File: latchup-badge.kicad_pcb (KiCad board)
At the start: 2 copper layers, 101.6 x 71.1 mm, 42 parts, among them J1 USB_B_Micro, J2 Connector_Generic:Conn_02x06_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, J3 Connector_Generic:Conn_02x06_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, J4 Connector_Generic:Conn_02x05_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, SW1 SW_Push, SW2 SW_Push, U1 ICE40UP5K-SG48ITR, U2 TLV70012_SOT23-5, U3 TLV70033_SOT23-5, U4 M25PX32-VMW, X1 ASE-12.000MHz

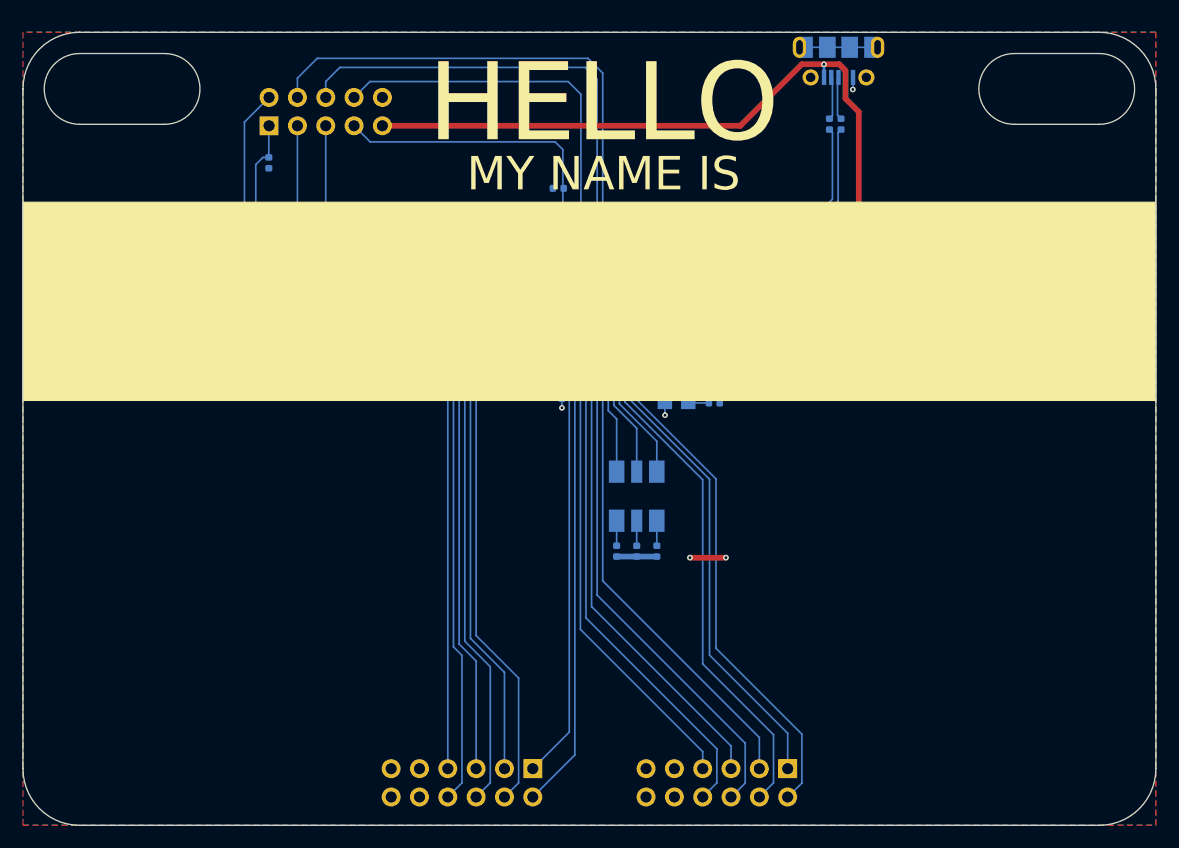
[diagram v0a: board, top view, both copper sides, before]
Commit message: Switch to USB-C connector and shrink board
Signed-off-by: Michael Welling <mwelling@ieee.org>
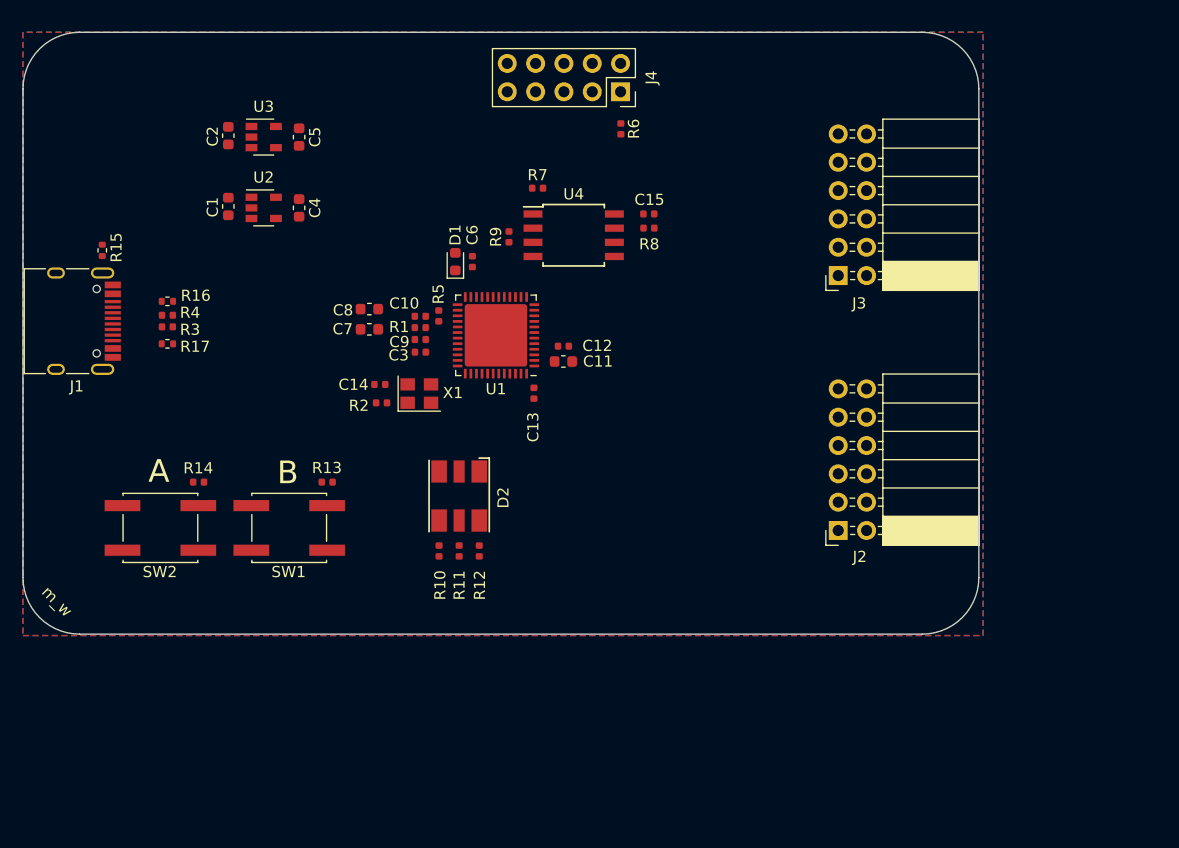
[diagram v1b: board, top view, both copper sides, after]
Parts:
- added R15: 1M, Resistor_SMD:R_0402_1005Metric, F.Cu at (83.3, 70.4)
- added R16: 5.1K, Resistor_SMD:R_0402_1005Metric, F.Cu at (89.2, 74.9)
- added R17: 5.1K, Resistor_SMD:R_0402_1005Metric, F.Cu at (89.2, 78.7)
- C1, C10, C11, C12, C13, C14, C15, C2, C3, C4, C5, C6, C7, C8, C9, D1, D2, J2, J3, J4, R1, R10, R11, R12, R13, R14, R2, R3, R4, R5, R6, R7, R8, R9, SW1, SW2, U1, U2, U3, U4, X1: moved to F.Cu
- J1: value USB_B_Micro -> USB_C_Receptacle_USB2.0; footprint Connector_USB:USB_Micro-B_Molex-105017-0001 -> Connector_USB:USB_C_Receptacle_HRO_TYPE-C-31-M-12; moved to F.Cu
- moved SW2 85.1 mm to (88.5, 95.2), turned to 180 degrees
- moved R14 78.4 mm to (92.0, 91.1), turned to 180 degrees
- moved J1 73.0 mm to (80.2, 76.7), turned to -90 degrees
- moved R3 63.1 mm to (89.2, 77.2), turned to 180 degrees
- moved SW1 62.8 mm to (100.1, 95.2), turned to 180 degrees
- moved R4 61.8 mm to (89.2, 76.2), turned to 180 degrees
- moved C1 56.5 mm to (94.6, 66.4)
- moved C2 56.5 mm to (94.6, 60.1)
- moved R13 56.4 mm to (103.5, 91.1), turned to 180 degrees
- moved J3 52.0 mm to (149.3, 72.6), turned to 180 degrees
- moved U2 50.4 mm to (97.8, 66.5), turned to 0 degrees
- moved U3 50.4 mm to (97.8, 60.2), turned to 0 degrees
- moved C4 44.3 mm to (101.0, 66.5)
- moved C5 44.3 mm to (101.0, 60.2)
- moved C7 32.0 mm to (107.3, 77.4), turned to 180 degrees
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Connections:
- R3 pad 1: /USBD+ -> /USBD-
- R3 pad 2: Net-(J1-Pad3) -> Net-(R3-Pad2)
- R4 pad 1: /USBD- -> /USBD+
- R4 pad 2: Net-(J1-Pad2) -> Net-(R4-Pad2)
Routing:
- net +5V: track 81.3 -> 0.00 mm, vias 2 -> 0
- net /J3_P8: track 54.4 -> 0.00 mm
- net /J3_P6: track 53.0 -> 0.00 mm
- net /J3_P7: track 52.9 -> 0.00 mm
- net /J3_P5: track 50.6 -> 0.00 mm
- net /J3_P4: track 50.6 -> 0.00 mm
- net /TX: track 50.5 -> 0.00 mm
- net /J3_P3: track 49.3 -> 0.00 mm
- net /BTN_A: track 48.9 -> 0.00 mm, vias 2 -> 0
- net /CDONE: track 47.2 -> 0.00 mm, vias 2 -> 0
- net /RX: track 46.3 -> 0.00 mm
- net /ICE40_SPI_SI: track 45.8 -> 0.00 mm
- net /J2_P2: track 45.3 -> 0.00 mm
- net /J2_P4: track 44.0 -> 0.00 mm
- net /J2_P6: track 44.0 -> 0.00 mm
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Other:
- board size 101.6 x 71.1 mm -> 85.7 x 54 mm
- board text removed: "HELLO"
- board text removed: "MY NAME IS"
- board text removed: "PCB Sponsored by:"

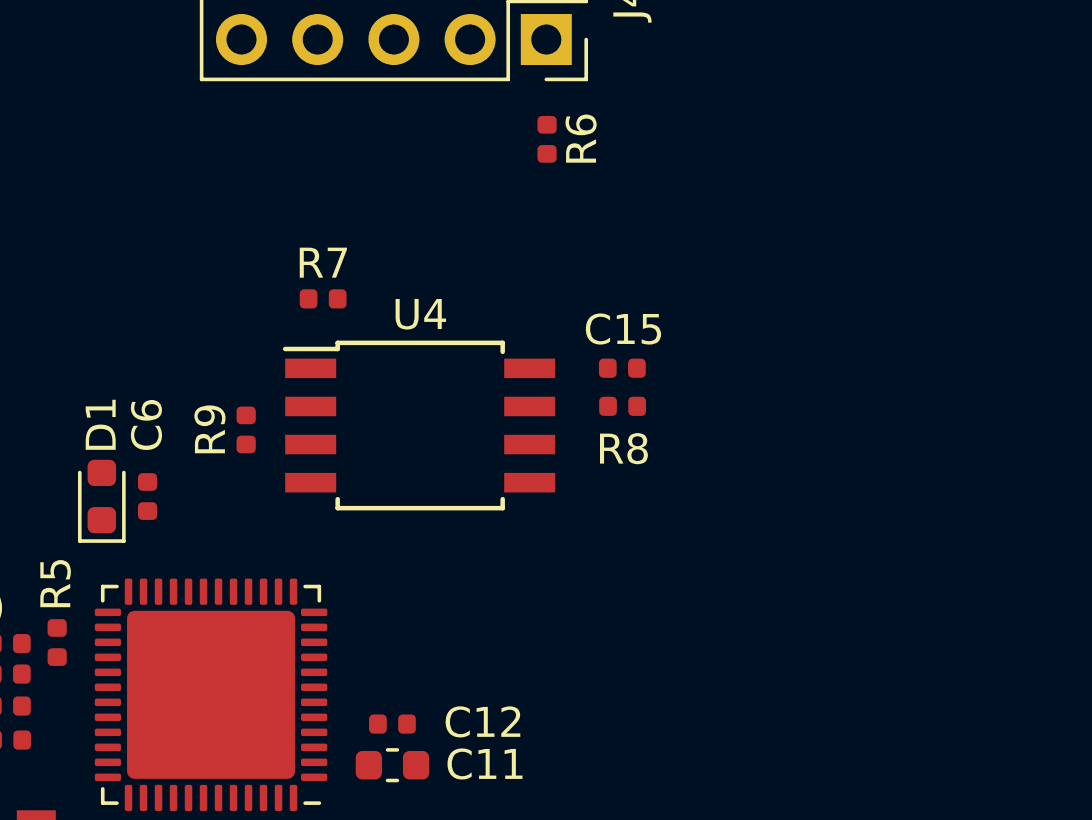
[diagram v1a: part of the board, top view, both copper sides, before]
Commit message: Add PSRAM
Signed-off-by: Michael Welling <mwelling@ieee.org>
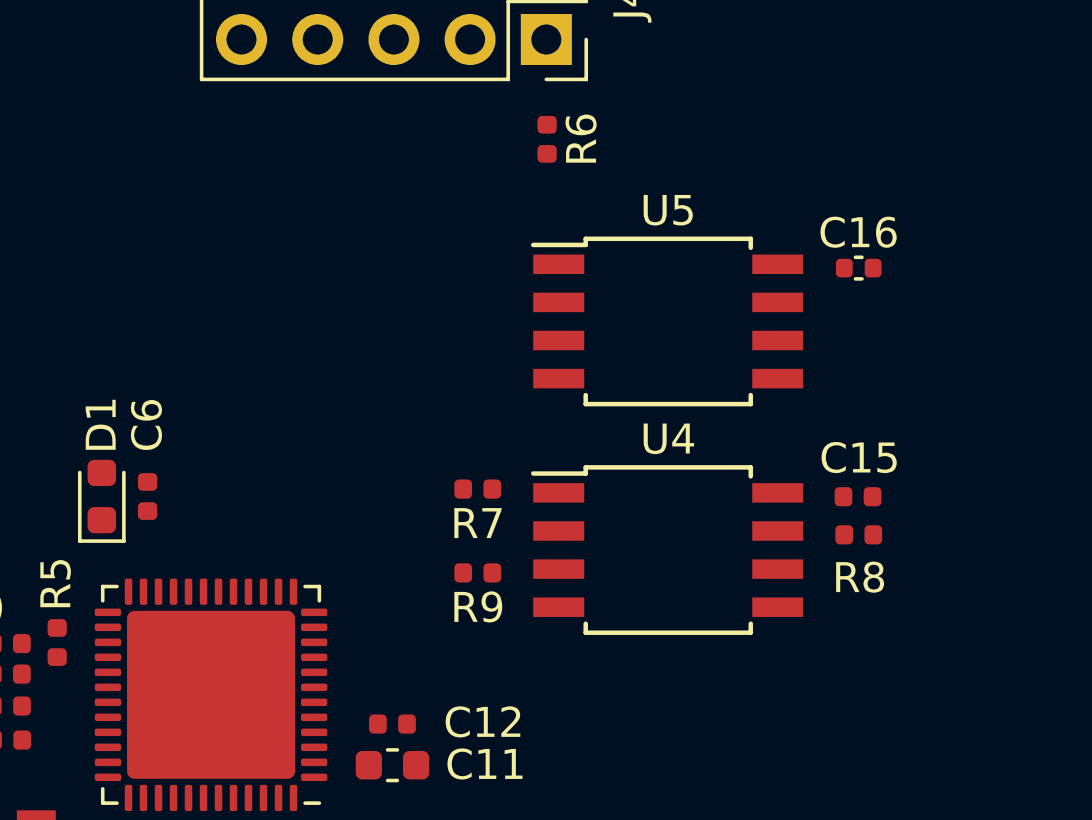
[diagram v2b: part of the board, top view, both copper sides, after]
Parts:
- added C16: .1uF, Capacitor_SMD:C_0402_1005Metric, F.Cu at (140.2, 63.8)
- added U5: LY68L6400, Package_SO:SOIC-8W_5.3x5.3mm_P1.27mm, F.Cu at (133.9, 65.5)
- U4: footprint Package_SO:SOIJ-8_5.3x5.3mm_P1.27mm -> Package_SO:SOIC-8W_5.3x5.3mm_P1.27mm
- moved U4 9.25 mm to (133.9, 73.2)
- moved R9 9.07 mm to (127.5, 73.9), turned to 180 degrees
- moved R8 8.96 mm to (140.2, 72.6)
- moved C15 8.95 mm to (140.2, 71.4)
- moved R7 8.17 mm to (127.5, 71.1), turned to 180 degrees
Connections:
- U1 pad 3: unconnected-(U1-Pad3) -> /SS_PSRAM

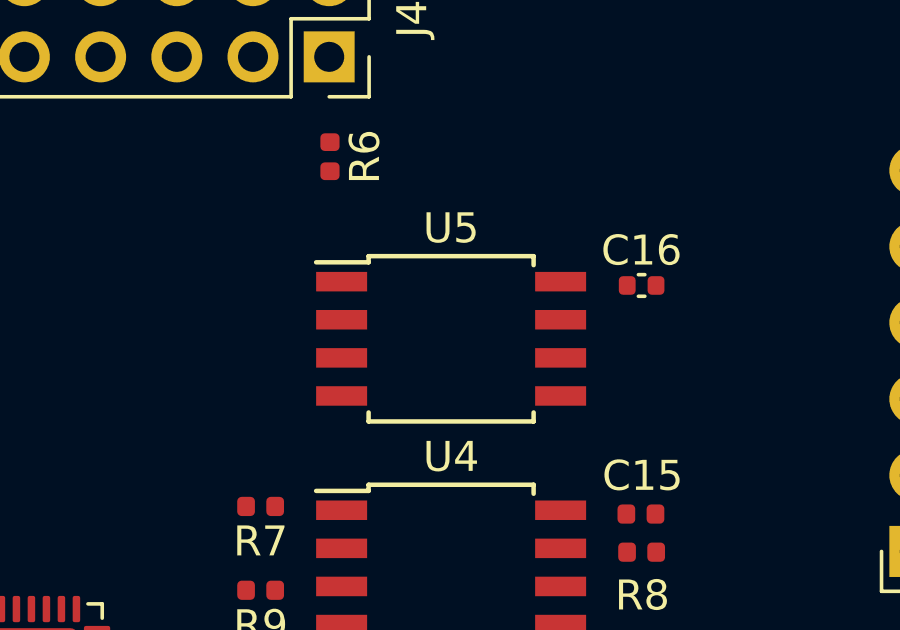
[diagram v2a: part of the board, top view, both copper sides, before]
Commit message: Update PSRAM footprint
Signed-off-by: Michael Welling <mwelling@ieee.org>
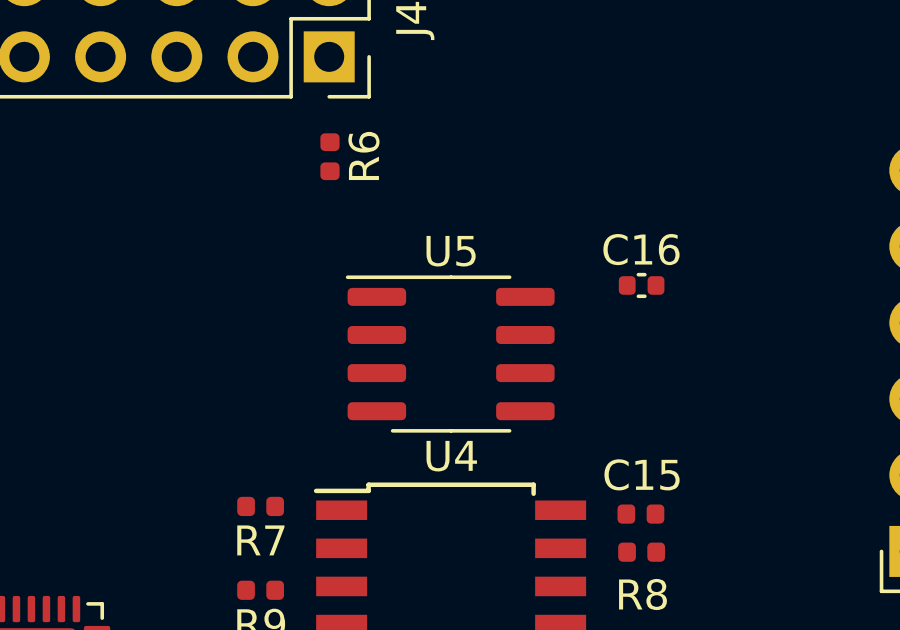
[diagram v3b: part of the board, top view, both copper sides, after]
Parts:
- U5: footprint Package_SO:SOIC-8W_5.3x5.3mm_P1.27mm -> Package_SO:SOIC-8_3.9x4.9mm_P1.27mm
- moved U5 0.51 mm to (133.9, 66.0)
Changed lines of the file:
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@@
     )
   )
-  (footprint "Package_SO:SOIC-8W_5.3x5.3mm_P1.27mm" (layer "F.Cu")
-    (at 133.858 65.532)
-    (descr "8-Lead Plastic Small Outline (SM) - 5.28 mm Body [SOIC] (http://ww1.microchip.com/downloads/en/PackagingSpec/00000049BQ.pdf)")
-    (tags "SOIC 1.27")
+  (footprint "Package_SO:SOIC-8_3.9x4.9mm_P1.27mm" (layer "F.Cu")
+    (at 133.858 66.04)
+    (descr "SOIC, 8 Pin (JEDEC MS-012AA, https://www.analog.com/media/en/package-pcb-resources/package/pkg_pdf/soic_narrow-r/r_8.pdf), generated with kicad-footprint-generator ipc_gullwing_generator.py")
+    (tags "SOIC SO")
     (property "Sheetfile" "latchup-badge.kicad_sch")
     (property "Sheetname" "")
     (attr smd)
-    (fp_text reference "U5" (at 0 -3.68) (layer "F.SilkS")
+    (fp_text reference "U5" (at 0 -3.4) (layer "F.SilkS")
       (effects (font (size 1 1) (thickness 0.15)))
     )
-    (fp_text value "LY68L6400" (at 0 3.68) (layer "F.Fab")
+    (fp_text value "LY68L6400" (at 0 3.4) (layer "F.Fab")
       (effects (font (size 1 1) (thickness 0.15)))
     )
     (fp_text user "${REFERENCE}" (at 0 0) (layer "F.Fab")
-      (effects (font (size 1 1) (thickness 0.15)))
+      (effects (font (size 0.98 0.98) (thickness 0.15)))
     )
-    (fp_line (start -2.75 2.755) (end 2.75 2.755) (layer "F.SilkS") (width 0.15))
-    (fp_line (start -2.75 -2.755) (end -2.75 -2.55) (layer "F.SilkS") (width 0.15))
-    (fp_line (start -2.75 -2.55) (end -4.5 -2.55) (layer "F.SilkS") (width 0.15))
-    (fp_line (start 2.75 -2.755) (end 2.75 -2.455) (layer "F.SilkS") (width 0.15))
-    (fp_line (start -2.75 2.755) (end -2.75 2.455) (layer "F.SilkS") (width 0.15))
-    (fp_line (start -2.75 -2.755) (end 2.75 -2.755) (layer "F.SilkS") (width 0.15))
-    (fp_line (start 2.75 2.755) (end 2.75 2.455) (layer "F.SilkS") (width 0.15))
-    (fp_line (start -4.75 2.95) (end 4.75 2.95) (layer "F.CrtYd") (width 0.05))
-    (fp_line (start -4.75 -2.95) (end -4.75 2.95) (layer "F.CrtYd") (width 0.05))
-    (fp_line (start -4.75 -2.95) (end 4.75 -2.95) (layer "F.CrtYd") (width 0.05))
-    (fp_line (start 4.75 -2.95) (end 4.75 2.95) (layer "F.CrtYd") (width 0.05))
-    (fp_line (start -1.65 -2.65) (end 2.65 -2.65) (layer "F.Fab") (width 0.15))
-    (fp_line (start 2.65 2.65) (end -2.65 2.65) (layer "F.Fab") (width 0.15))
-    (fp_line (start -2.65 -1.65) (end -1.65 -2.65) (layer "F.Fab") (width 0.15))
-    (fp_line (start 2.65 -2.65) (end 2.65 2.65) (layer "F.Fab") (width 0.15))
-    (fp_line (start -2.65 2.65) (end -2.65 -1.65) (layer "F.Fab") (width 0.15))
-    (pad "1" smd rect (at -3.65 -1.905) (size 1.7 0.65) (layers "F.Cu" "F.Paste" "F.Mask")
+    (fp_line (start 0 -2.56) (end -3.45 -2.56) (layer "F.SilkS") (width 0.12))
+    (fp_line (start 0 2.56) (end 1.95 2.56) (layer "F.SilkS") (width 0.12))
+    (fp_line (start 0 2.56) (end -1.95 2.56) (layer "F.SilkS") (width 0.12))
+    (fp_line (start 0 -2.56) (end 1.95 -2.56) (layer "F.SilkS") (width 0.12))
+    (fp_line (start -3.7 -2.7) (end -3.7 2.7) (layer "F.CrtYd") (width 0.05))
+    (fp_line (start -3.7 2.7) (end 3.7 2.7) (layer "F.CrtYd") (width 0.05))
+    (fp_line (start 3.7 -2.7) (end -3.7 -2.7) (layer "F.CrtYd") (width 0.05))
+    (fp_line (start 3.7 2.7) (end 3.7 -2.7) (layer "F.CrtYd") (width 0.05))
+    (fp_line (start -0.975 -2.45) (end 1.95 -2.45) (layer "F.Fab") (width 0.1))
+    (fp_line (start -1.95 2.45) (end -1.95 -1.475) (layer "F.Fab") (width 0.1))
+    (fp_line (start 1.95 2.45) (end -1.95 2.45) (layer "F.Fab") (width 0.1))
+    (fp_line (start 1.95 -2.45) (end 1.95 2.45) (layer "F.Fab") (width 0.1))
+    (fp_line (start -1.95 -1.475) (end -0.975 -2.45) (layer "F.Fab") (width 0.1))
+    (pad "1" smd roundrect (at -2.475 -1.905) (size 1.95 0.6) (layers "F.Cu" "F.Paste" "F.Mask") (roundrect_rratio 0.25)
       (net 4 "/SS_PSRAM") (pinfunction "S#") (pintype "input"))
-    (pad "2" smd rect (at -3.65 -0.635) (size 1.7 0.65) (layers "F.Cu" "F.Paste" "F.Mask")
+    (pad "2" smd roundrect (at -2.475 -0.635) (size 1.95 0.6) (layers "F.Cu" "F.Paste" "F.Mask") (roundrect_rratio 0.25)
       (net 17 "/ICE40_SPI_SI") (pinfunction "DQ1") (pintype "bidirectional"))
-    (pad "3" smd rect (at -3.65 0.635) (size 1.7 0.65) (layers "F.Cu" "F.Paste" "F.Mask")
+    (pad "3" smd roundrect (at -2.475 0.635) (size 1.95 0.6) (layers "F.Cu" "F.Paste" "F.Mask") (roundrect_rratio 0.25)
       (net 48 "/FLASH_IO2_WP") (pinfunction "W#/VPP") (pintype "input"))
-    (pad "4" smd rect (at -3.65 1.905) (size 1.7 0.65) (layers "F.Cu" "F.Paste" "F.Mask")
+    (pad "4" smd roundrect (at -2.475 1.905) (size 1.95 0.6) (layers "F.Cu" "F.Paste" "F.Mask") (roundrect_rratio 0.25)
       (net 8 "GND") (pinfunction "VSS") (pintype "power_in"))
-    (pad "5" smd rect (at 3.65 1.905) (size 1.7 0.65) (layers "F.Cu" "F.Paste" "F.Mask")
+    (pad "5" smd roundrect (at 2.475 1.905) (size 1.95 0.6) (layers "F.Cu" "F.Paste" "F.Mask") (roundrect_rratio 0.25)
       (net 20 "/ICE40_SPI_SO") (pinfunction "DQ0") (pintype "bidirectional"))
-    (pad "6" smd rect (at 3.65 0.635) (size 1.7 0.65) (layers "F.Cu" "F.Paste" "F.Mask")
+    (pad "6" smd roundrect (at 2.475 0.635) (size 1.95 0.6) (layers "F.Cu" "F.Paste" "F.Mask") (roundrect_rratio 0.25)
       (net 19 "/ICE40_SPI_SCK") (pinfunction "C") (pintype "input"))
-    (pad "7" smd rect (at 3.65 -0.635) (size 1.7 0.65) (layers "F.Cu" "F.Paste" "F.Mask")
+    (pad "7" smd roundrect (at 2.475 -0.635) (size 1.95 0.6) (layers "F.Cu" "F.Paste" "F.Mask") (roundrect_rratio 0.25)
       (net 47 "/FLASH_IO3_HLD") (pinfunction "HOLD#") (pintype "input"))
-    (pad "8" smd rect (at 3.65 -1.905) (size 1.7 0.65) (layers "F.Cu" "F.Paste" "F.Mask")
+    (pad "8" smd roundrect (at 2.475 -1.905) (size 1.95 0.6) (layers "F.Cu" "F.Paste" "F.Mask") (roundrect_rratio 0.25)
       (net 10 "+3V3") (pinfunction "VCC") (pintype "power_in"))
-    (model "${KICAD6_3DMODEL_DIR}/Package_SO.3dshapes/SOIC-8W_5.3x5.3mm_P1.27mm.wrl"
+    (model "${KICAD6_3DMODEL_DIR}/Package_SO.3dshapes/SOIC-8_3.9x4.9mm_P1.27mm.wrl"
       (offset (xyz 0 0 0))
       (scale (xyz 1 1 1))
